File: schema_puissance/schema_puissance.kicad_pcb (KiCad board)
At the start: 2 copper layers, 100 x 181.5 mm, 52 parts, among them Q1 PN2222A, Q2 PN2222A, Q3 PN2222A, Q4 PN2222A, Q5 PN2222A, Q6 PN2222A, Q7 PN2222A, Q8 PN2222A, U1 FOD814A, U10 RT114, U11 FOD814A, U12 RT114, U13 FOD814A, U14 RT114, U15 FOD814A, U16 RT114, U2 RT114, U3 FOD814A, U4 RT114, U5 FOD814A, U6 RT114, U7 FOD814A, U8 RT114, U9 FOD814A

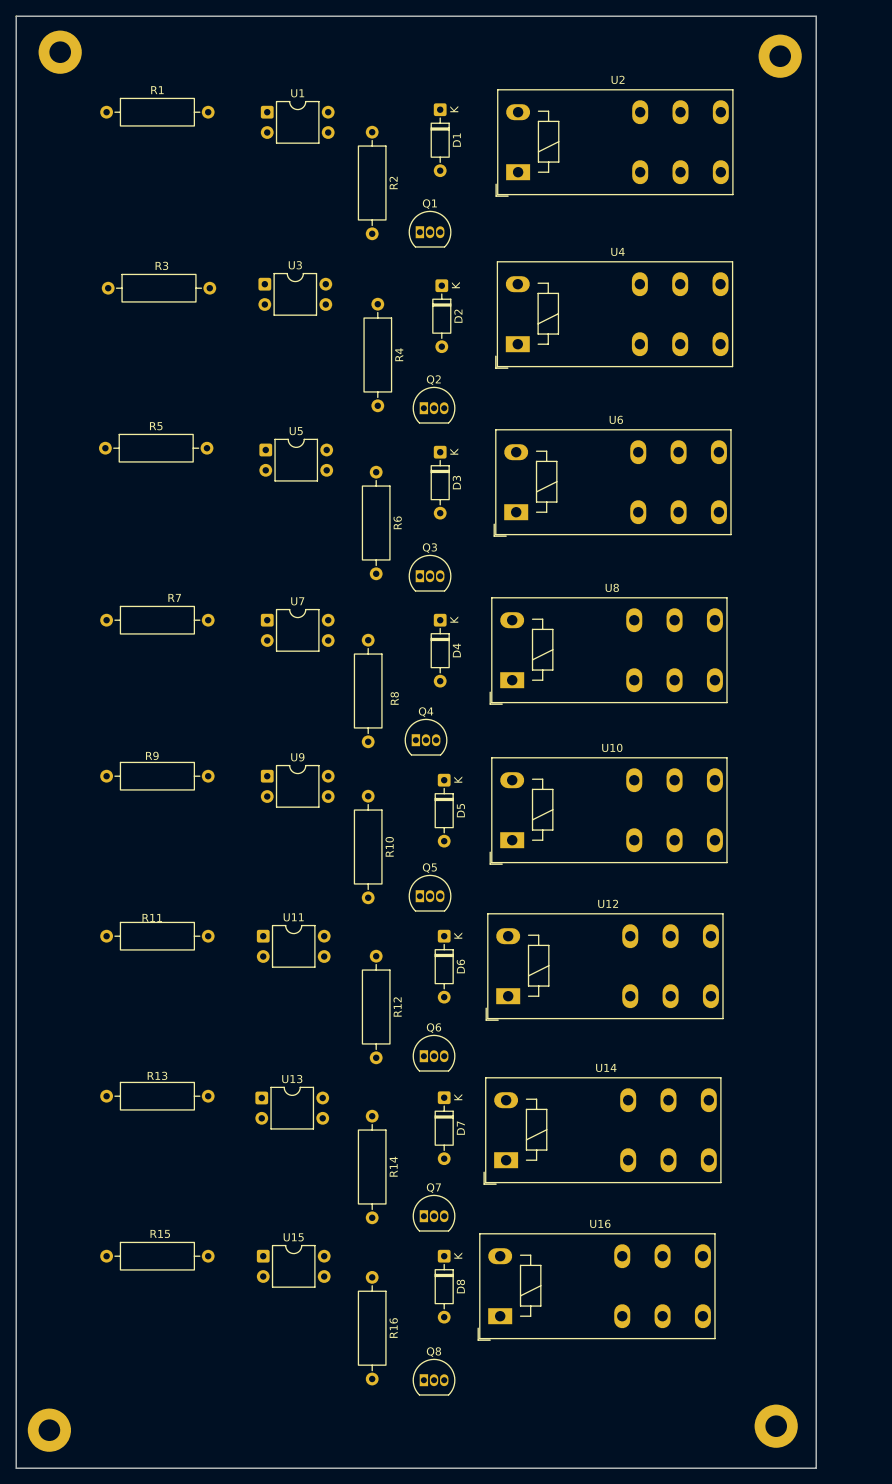
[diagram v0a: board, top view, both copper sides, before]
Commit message: Modification 3 : connecteurs mis, routes tracées, layers faits. Il manque le connecteur pour les input et comment les relier au input
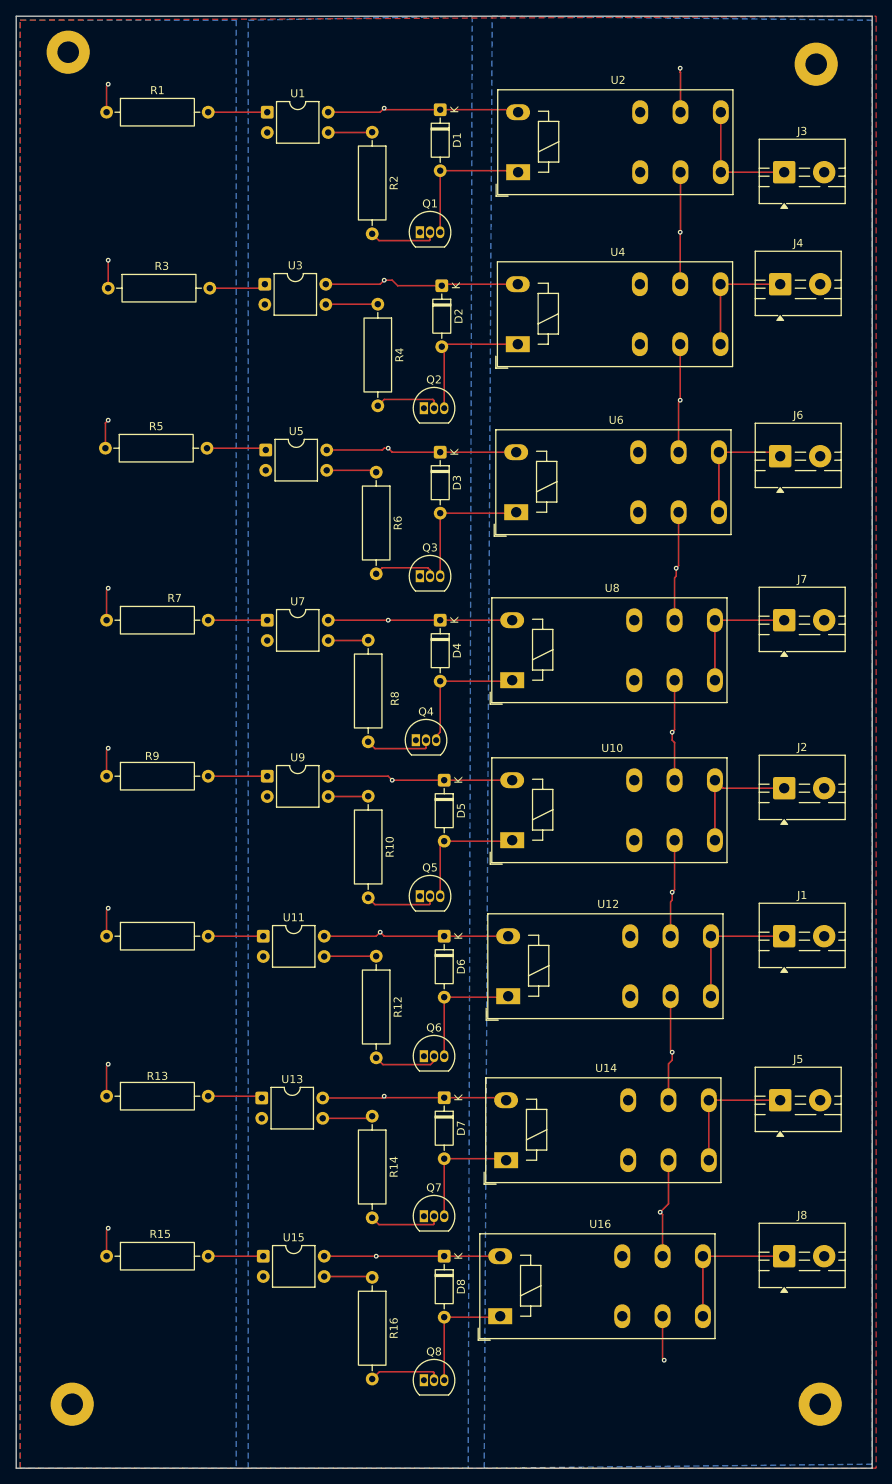
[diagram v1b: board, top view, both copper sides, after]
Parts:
- added J1: Conn_01x02, TerminalBlock:TerminalBlock_MaiXu_MX126-5.0-02P_1x02_P5.00mm, F.Cu at (116.0, 127.5)
- added J2: Conn_01x02, TerminalBlock:TerminalBlock_MaiXu_MX126-5.0-02P_1x02_P5.00mm, F.Cu at (116.0, 109.0)
- added J3: Conn_01x02, TerminalBlock:TerminalBlock_MaiXu_MX126-5.0-02P_1x02_P5.00mm, F.Cu at (116.0, 32.0)
- added J4: Conn_01x02, TerminalBlock:TerminalBlock_MaiXu_MX126-5.0-02P_1x02_P5.00mm, F.Cu at (115.5, 46.0)
- added J5: Conn_01x02, TerminalBlock:TerminalBlock_MaiXu_MX126-5.0-02P_1x02_P5.00mm, F.Cu at (115.5, 148.0)
- added J6: Conn_01x02, TerminalBlock:TerminalBlock_MaiXu_MX126-5.0-02P_1x02_P5.00mm, F.Cu at (115.5, 67.5)
- added J7: Conn_01x02, TerminalBlock:TerminalBlock_MaiXu_MX126-5.0-02P_1x02_P5.00mm, F.Cu at (116.0, 88.0)
- added J8: Conn_01x02, TerminalBlock:TerminalBlock_MaiXu_MX126-5.0-02P_1x02_P5.00mm, F.Cu at (116.0, 167.5)
- moved H4 6.15 mm to (120.5, 186.0)
- moved H2 4.61 mm to (120.0, 18.5)
- moved H3 4.32 mm to (27.0, 186.0)
- moved H1 1.00 mm to (26.5, 17.0)
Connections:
- net /VDD 5 renamed VCC 5V
- U10 pad 11: unconnected-(U10-Pad11) -> VCC 24V
- U10 pad 14: unconnected-(U10-Pad14) -> Net-(J2-Pin_1)
- U10 pad 21: unconnected-(U10-Pad21) -> VCC 24V
- U10 pad 24: unconnected-(U10-Pad24) -> Net-(J2-Pin_1)
- U12 pad 11: unconnected-(U12-Pad11) -> VCC 24V
- U12 pad 14: unconnected-(U12-Pad14) -> Net-(J1-Pin_1)
- U12 pad 21: unconnected-(U12-Pad21) -> VCC 24V
- U12 pad 24: unconnected-(U12-Pad24) -> Net-(J1-Pin_1)
- U14 pad 11: unconnected-(U14-Pad11) -> VCC 24V
- U14 pad 14: unconnected-(U14-Pad14) -> Net-(J5-Pin_1)
- U14 pad 21: unconnected-(U14-Pad21) -> VCC 24V
- U14 pad 24: unconnected-(U14-Pad24) -> Net-(J5-Pin_1)
- U16 pad 11: unconnected-(U16-Pad11) -> VCC 24V
- U16 pad 14: unconnected-(U16-Pad14) -> Net-(J8-Pin_1)
- U16 pad 21: unconnected-(U16-Pad21) -> VCC 24V
- U16 pad 24: unconnected-(U16-Pad24) -> Net-(J8-Pin_1)
- U2 pad 11: unconnected-(U2-Pad11) -> VCC 24V
- U2 pad 14: unconnected-(U2-Pad14) -> Net-(J3-Pin_1)
- U2 pad 21: unconnected-(U2-Pad21) -> VCC 24V
- U2 pad 24: unconnected-(U2-Pad24) -> Net-(J3-Pin_1)
- U4 pad 11: unconnected-(U4-Pad11) -> VCC 24V
- U4 pad 14: unconnected-(U4-Pad14) -> Net-(J4-Pin_1)
- U4 pad 21: unconnected-(U4-Pad21) -> VCC 24V
- U4 pad 24: unconnected-(U4-Pad24) -> Net-(J4-Pin_1)
- U6 pad 11: unconnected-(U6-Pad11) -> VCC 24V
- U6 pad 14: unconnected-(U6-Pad14) -> Net-(J6-Pin_1)
- U6 pad 21: unconnected-(U6-Pad21) -> VCC 24V
- U6 pad 24: unconnected-(U6-Pad24) -> Net-(J6-Pin_1)
- U8 pad 11: unconnected-(U8-Pad11) -> VCC 24V
- U8 pad 14: unconnected-(U8-Pad14) -> Net-(J7-Pin_1)
- U8 pad 21: unconnected-(U8-Pad21) -> VCC 24V
- U8 pad 24: unconnected-(U8-Pad24) -> Net-(J7-Pin_1)
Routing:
- net VCC 5V: track 0.00 -> 187.6 mm, vias 0 -> 8
- net VCC 24V: track 0.00 -> 103.2 mm, vias 0 -> 9
- net VCC 3.3V: track 0.00 -> 29.6 mm, vias 0 -> 8
- net Net-(J8-Pin_1): track 0.00 -> 17.7 mm
- net Net-(D1-A): track 0.00 -> 17.5 mm
- net Net-(D2-A): track 0.00 -> 17.4 mm
- net Net-(D3-A): track 0.00 -> 17.4 mm
- net Net-(J1-Pin_1): track 0.00 -> 16.7 mm
- net Net-(D4-A): track 0.00 -> 16.6 mm
- net Net-(J2-Pin_1): track 0.00 -> 16.6 mm
- net Net-(J5-Pin_1): track 0.00 -> 16.4 mm
- net Net-(J7-Pin_1): track 0.00 -> 16.2 mm
- net Net-(D5-A): track 0.00 -> 15.6 mm
- net Net-(D6-A): track 0.00 -> 15.4 mm
- net Net-(J3-Pin_1): track 0.00 -> 15.4 mm
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- added copper zone on F.Cu, net GND
- added copper zone on B.Cu, net VCC 24V
- added copper zone on B.Cu, net VCC 3.3V
- added copper zone on B.Cu, net VCC 5V
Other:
- board size 100 x 181.5 mm -> 107 x 181.5 mm
